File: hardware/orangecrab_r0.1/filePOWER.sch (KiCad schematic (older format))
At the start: 5 parts

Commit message: Initial Routing of Memory Traces. Wired up DCDC converters.
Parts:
- removed U? (x2): FAN53601, symbol gkl_pmic:FAN53601
- added C10: 0.22uF, Capacitor_SMD:C_0201_0603Metric, symbol Device:C
- added C11, C15, C16, C17, C18, C6, C7, C8: 10uF, Capacitor_SMD:C_0402_1005Metric, symbol Device:C
- added C12, C13: 4.7uF, Capacitor_SMD:C_0402_1005Metric, symbol Device:C
- added C14, C2, C5: 10nF, Capacitor_SMD:C_0201_0603Metric, symbol Device:C
- added C3: 10uF, Capacitor_SMD:C_0603_1608Metric, symbol Device:C
- added C9: 0.1uF, Capacitor_SMD:C_0201_0603Metric, symbol Device:C
- added D2: RED, symbol Device:LED_ALT
- added D3: GREEN, symbol Device:LED_ALT
- added L1, L2, L3: 470uH, Inductor_SMD:L_0805_2012Metric, symbol Device:L_Small
- added R1, R13, R14, R17, R18, R5: 100k, Resistor_SMD:R_0201_0603Metric, symbol Device:R
- added R10, R11, R12, R9: 0, symbol Device:R
- added R15, R16, R2: 115k, Resistor_SMD:R_0201_0603Metric, symbol Device:R
- added R6: 0R, symbol Device:R
- added R7, R8: 1k5, symbol Device:R
- added U1, U2, U7: FAN53541, Package_CSP:WLCSP-20_1.934x2.434mm_Layout4x5_P0.4mm, symbol gkl_pmic:FAN53541
- added U8: TPS51206, Package_DFN_QFN:DFN-10-1EP_3x3mm_P0.5mm_EP1.7x2.5mm, symbol gkl_pmic:TPS51206
- U5: renamed from U?; footprint (none) -> Package_DFN_QFN:QFN-16-1EP_3x3mm_P0.5mm_EP1.75x1.75mm
- gave numbers to parts that had none: 2
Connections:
- net labels added: GND, P1.1V, P1.5V, P3.3V, PGOOD_LAST, PGOOD_P1.1V, USB_DN, USB_DP, VSYS, VTT, VTT_REF
- wire segments 0 -> 286
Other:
- note added: "1.5V @ 5A\n- DDR3\n"
- note added: "3.3V @ 5A\n- System IO\n"
- note added: "DDR3 VTT Generator"
- note removed: "1.1V @ 1A"
- note removed: "1.35V @ 1A"
- moved on the sheet: J3, J5, U5

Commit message: Routed more FPGA signals
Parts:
- J3: footprint (none) -> Connector_USB:USB_Micro-B_Molex-105017-0001
- R10, R11, R12, R7, R8, R9: footprint (none) -> Resistor_SMD:R_0201_0603Metric
- R6: footprint (none) -> Resistor_SMD:R_0402_1005Metric
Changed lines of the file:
@@
 F 0 "R6" V 1493 5950 50  0000 C CNN
 F 1 "0R" V 1584 5950 50  0000 C CNN
-F 2 "" V 1630 5950 50  0001 C CNN
+F 2 "Resistor_SMD:R_0402_1005Metric" V 1630 5950 50  0001 C CNN
 F 3 "~" H 1700 5950 50  0001 C CNN
 	1    1700 5950
@@
 F 0 "R8" V 2815 900 50  0000 C CNN
 F 1 "1k5" V 2906 900 50  0000 C CNN
-F 2 "" V 2630 900 50  0001 C CNN
+F 2 "Resistor_SMD:R_0201_0603Metric" V 2630 900 50  0001 C CNN
 F 3 "~" H 2700 900 50  0001 C CNN
 	1    2700 900
@@
 F 0 "R7" V 2493 800 50  0000 C CNN
 F 1 "1k5" V 2584 800 50  0000 C CNN
-F 2 "" V 2630 800 50  0001 C CNN
+F 2 "Resistor_SMD:R_0201_0603Metric" V 2630 800 50  0001 C CNN
 F 3 "~" H 2700 800 50  0001 C CNN
 	1    2700 800
@@
 F 0 "J3" H 1057 2067 50  0000 C CNN
 F 1 "USB_B_Micro" H 1057 1976 50  0000 C CNN
-F 2 "" H 1150 1550 50  0001 C CNN
+F 2 "Connector_USB:USB_Micro-B_Molex-105017-0001" H 1150 1550 50  0001 C CNN
 F 3 "~" H 1150 1550 50  0001 C CNN
 	1    1000 1600
@@
 F 0 "R9" H 3681 2804 50  0000 R CNN
 F 1 "0" H 3681 2895 50  0000 R CNN
-F 2 "" V 3680 2850 50  0001 C CNN
+F 2 "Resistor_SMD:R_0201_0603Metric" V 3680 2850 50  0001 C CNN
 F 3 "~" H 3750 2850 50  0001 C CNN
 	1    3750 2850
@@
 F 0 "R10" H 3881 3054 50  0000 R CNN
 F 1 "0" H 3881 3145 50  0000 R CNN
-F 2 "" V 3880 3100 50  0001 C CNN
+F 2 "Resistor_SMD:R_0201_0603Metric" V 3880 3100 50  0001 C CNN
 F 3 "~" H 3950 3100 50  0001 C CNN
 	1    3950 3100
@@
 F 0 "R11" H 4081 2804 50  0000 R CNN
 F 1 "0" H 4081 2895 50  0000 R CNN
-F 2 "" V 4080 2850 50  0001 C CNN
+F 2 "Resistor_SMD:R_0201_0603Metric" V 4080 2850 50  0001 C CNN
 F 3 "~" H 4150 2850 50  0001 C CNN
 	1    4150 2850
@@
 F 0 "R12" H 4281 3054 50  0000 R CNN
 F 1 "0" H 4281 3145 50  0000 R CNN
-F 2 "" V 4280 3100 50  0001 C CNN
+F 2 "Resistor_SMD:R_0201_0603Metric" V 4280 3100 50  0001 C CNN
 F 3 "~" H 4350 3100 50  0001 C CNN
 	1    4350 3100

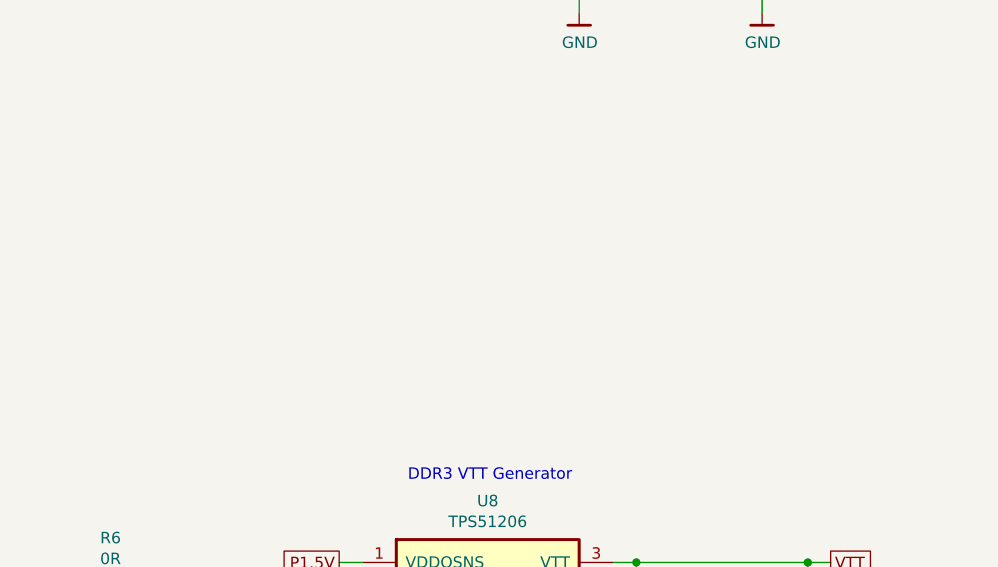
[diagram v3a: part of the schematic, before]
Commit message: Added 2.5V regulator. Completed more routing
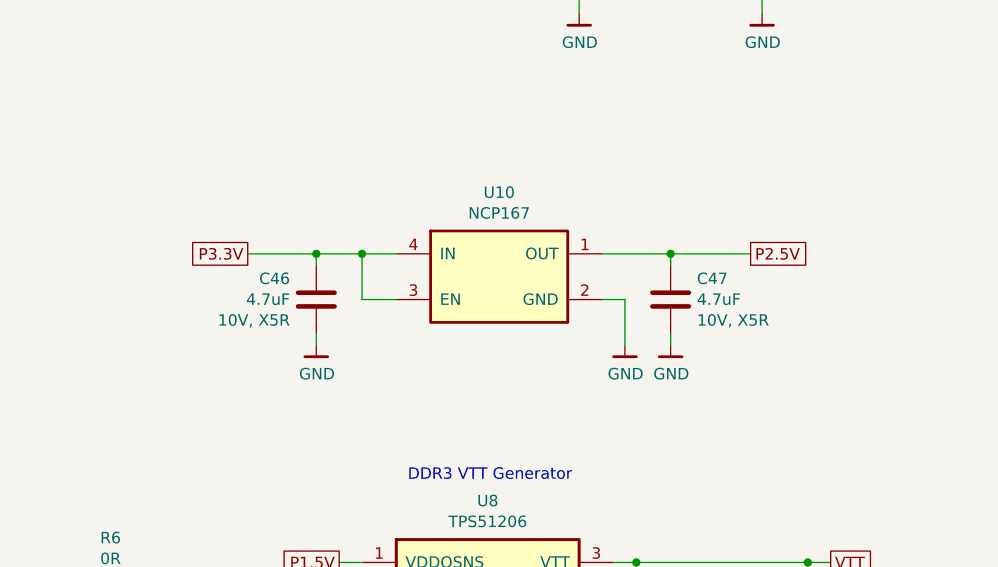
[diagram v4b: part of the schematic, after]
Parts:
- added C46, C47: 4.7uF, Capacitor_SMD:C_0402_1005Metric, symbol Device:C
- added U10: NCP167, gkl_housings_son:X2SON_4_1.0x1.0mm, symbol gkl_pmic:NCP167
- J5: footprint (none) -> gkl_conn:JST_PH_B2B-PH-SM4-TB_1x02-1MP_P2.00mm_Vertical
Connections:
- net GND: now also C46.2, C47.2, U10.2 (GND)
- net P3.3V: now also C46.1, U10.3 (EN), U10.4 (IN)
- new net P2.5V: C47.1, U10.1 (OUT)
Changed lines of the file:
@@
 F 0 "J5" H 5550 2200 50  0000 C CNN
 F 1 "Conn_01x02_Male" H 5300 2100 50  0000 C CNN
-F 2 "" H 5500 1900 50  0001 C CNN
+F 2 "gkl_conn:JST_PH_B2B-PH-SM4-TB_1x02-1MP_P2.00mm_Vertical" H 5500 1900 50  0001 C CNN
 F 3 "~" H 5500 1900 50  0001 C CNN
 	1    5500 1900
@@
 Wire Wire Line
 	7250 5300 7000 5300
+$Comp
+L gkl_pmic:NCP167 U10
+U 1 1 5D75643E
+P 3400 4600
+F 0 "U10" H 3400 4968 50  0000 C CNN
+F 1 "NCP167" H 3400 4877 50  0000 C CNN
+F 2 "gkl_housings_son:X2SON_4_1.0x1.0mm" H 3350 4950 50  0001 C CNN
+F 3 "" H 3400 4850 50  0001 C CNN
+	1    3400 4600
+	1    0    0    -1
+$EndComp
+Text GLabel 2300 4500 0    50   UnSpc ~ 0
+P3.3V
+$Comp
+L Device:C C46
+U 1 1 5D757AA5
+P 2600 4700
+F 0 "C46" H 2715 4791 50  0000 L CNN
+F 1 "4.7uF" H 2715 4700 50  0000 L CNN
+F 2 "Capacitor_SMD:C_0402_1005Metric" H 2638 4550 50  0001 C CNN
+F 3 "~" H 2600 4700 50  0001 C CNN
+F 4 "10V, X5R" H 2715 4609 50  0000 L CNN "Info"
+	1    2600 4700
+	-1   0    0    -1
+$EndComp
+$Comp
+L Device:C C47
+U 1 1 5D7582AA
+P 4150 4700
+F 0 "C47" H 4265 4791 50  0000 L CNN
+F 1 "4.7uF" H 4265 4700 50  0000 L CNN
+F 2 "Capacitor_SMD:C_0402_1005Metric" H 4188 4550 50  0001 C CNN
+F 3 "~" H 4150 4700 50  0001 C CNN
+F 4 "10V, X5R" H 4265 4609 50  0000 L CNN "Info"
+	1    4150 4700
+	1    0    0    -1
+$EndComp
+Text GLabel 4500 4500 2    50   UnSpc ~ 0
+P2.5V
+Wire Wire Line
+	3850 4500 4150 4500
+Wire Wire Line
+	4150 4550 4150 4500
+Connection ~ 4150 4500
+Wire Wire Line
+	4150 4500 4500 4500
+Wire Wire Line
+	2950 4500 2800 4500
+Wire Wire Line
+	2600 4550 2600 4500
+Connection ~ 2600 4500
+Wire Wire Line
+	2600 4500 2300 4500
+Wire Wire Line
+	2600 4850 2600 4900
+Wire Wire Line
+	4150 4850 4150 4900
+Wire Wire Line
+	3850 4700 3950 4700
+Wire Wire Line
+	3950 4700 3950 4900
+Wire Wire Line
+	2950 4700 2800 4700
+Wire Wire Line
+	2800 4700 2800 4500
+Connection ~ 2800 4500
+Wire Wire Line
+	2800 4500 2600 4500
+$Comp
+L gkl_power:GND #PWR0145
+U 1 1 5D85A10F
+P 2600 4900
+F 0 "#PWR0145" H 2600 4650 50  0001 C CNN
+F 1 "GND" H 2603 4774 50  0000 C CNN
+F 2 "" H 2500 4550 50  0001 C CNN
+F 3 "" H 2600 4900 50  0001 C CNN
+	1    2600 4900
+	1    0    0    -1
+$EndComp
+$Comp
+L gkl_power:GND #PWR0146
+U 1 1 5D85A3FC
+P 4150 4900
+F 0 "#PWR0146" H 4150 4650 50  0001 C CNN
+F 1 "GND" H 4153 4774 50  0000 C CNN
+F 2 "" H 4050 4550 50  0001 C CNN
+F 3 "" H 4150 4900 50  0001 C CNN
+	1    4150 4900
+	1    0    0    -1
+$EndComp
+$Comp
+L gkl_power:GND #PWR0147
+U 1 1 5D85A78D
+P 3950 4900
+F 0 "#PWR0147" H 3950 4650 50  0001 C CNN
+F 1 "GND" H 3953 4774 50  0000 C CNN
+F 2 "" H 3850 4550 50  0001 C CNN
+F 3 "" H 3950 4900 50  0001 C CNN
+	1    3950 4900
+	1    0    0    -1
+$EndComp
 $EndSCHEMATC

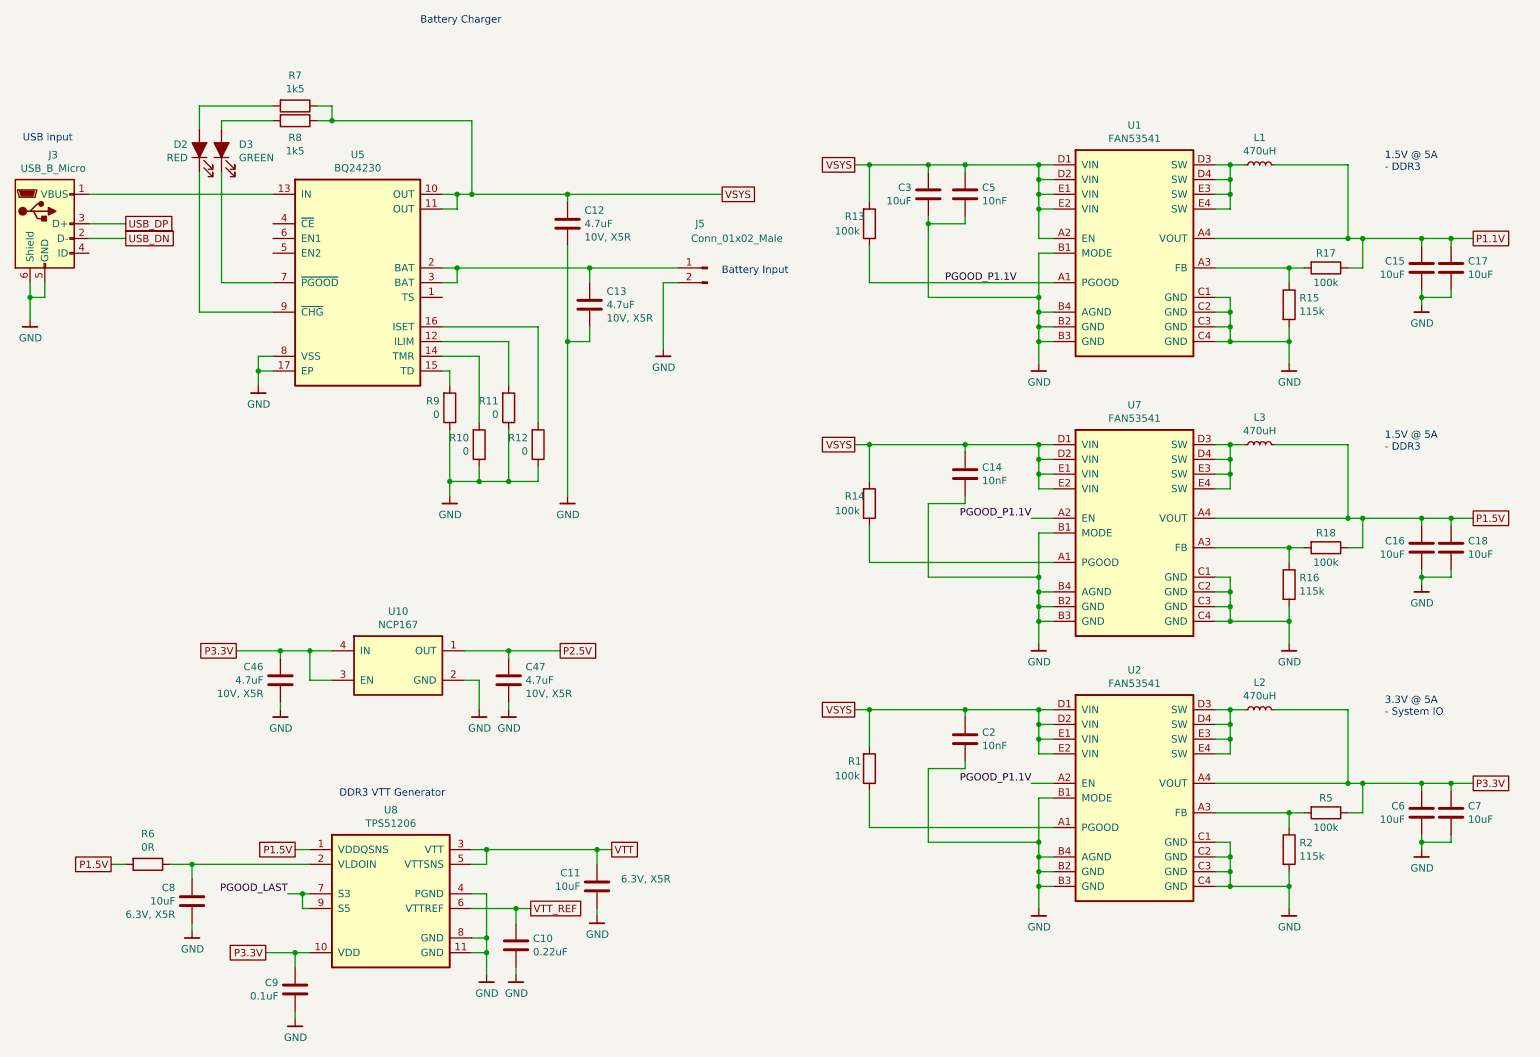
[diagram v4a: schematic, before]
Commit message: Added loads of decoupling capacitors. Added SD card. Started planning out power plane
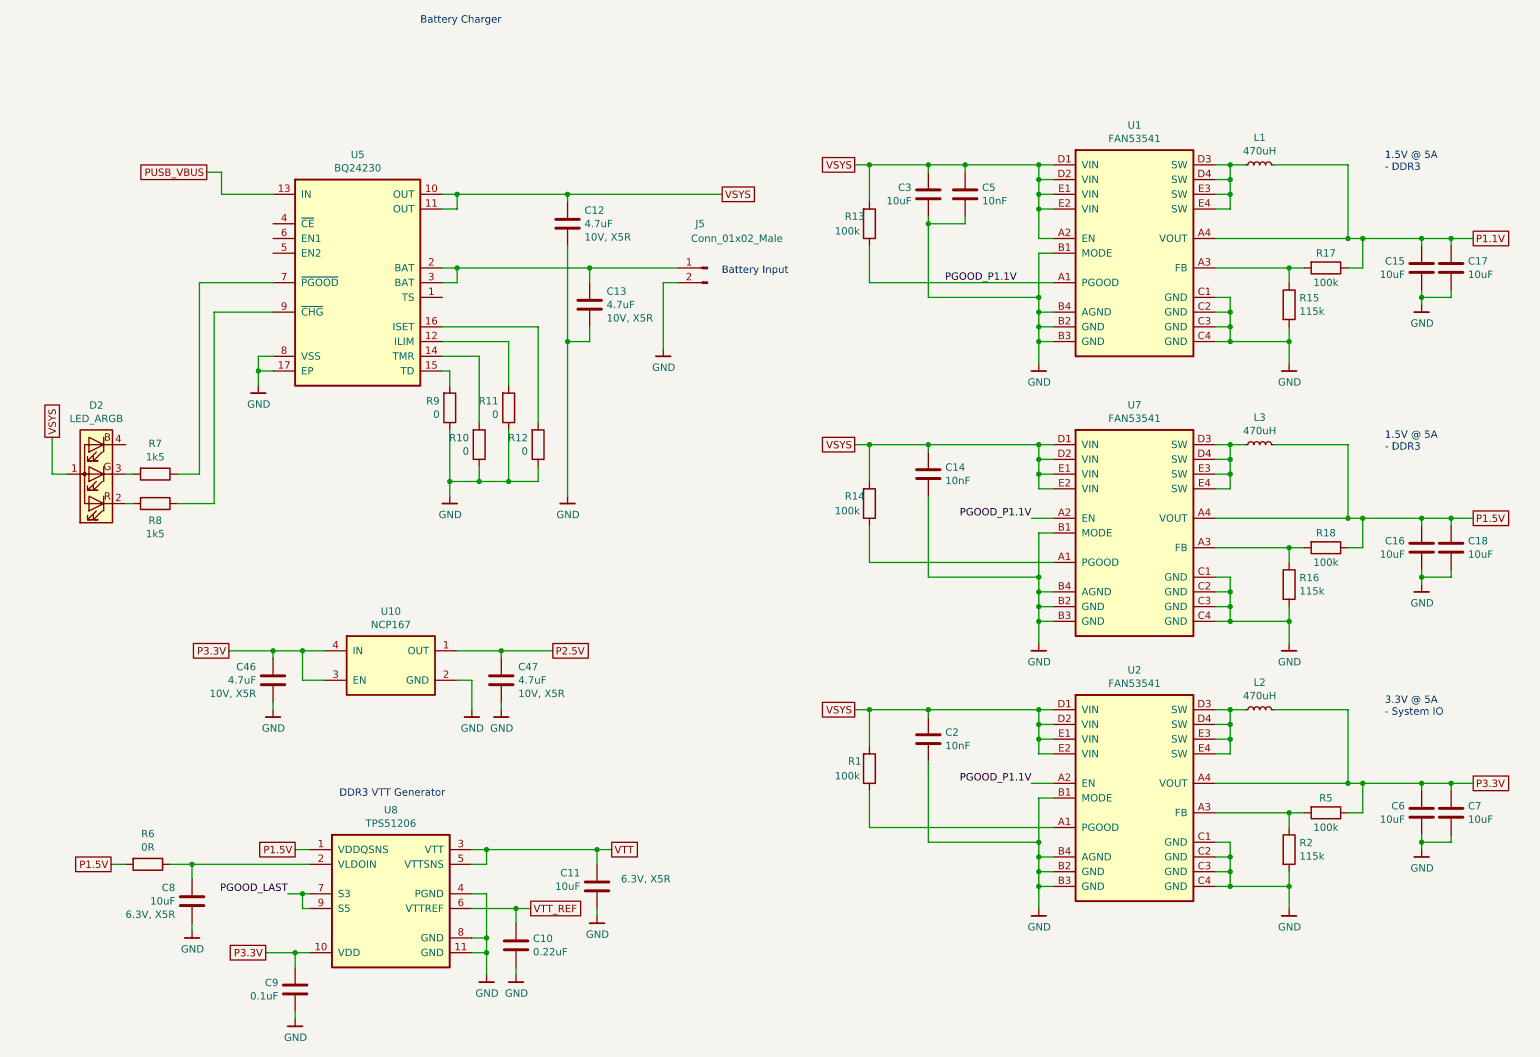
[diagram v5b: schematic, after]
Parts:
- removed D2: RED, symbol Device:LED_ALT
- removed D3: GREEN, symbol Device:LED_ALT
- removed J3: USB_B_Micro, Connector_USB:USB_Micro-B_Molex-105017-0001, symbol Connector:USB_B_Micro
- added D2: LED_ARGB, gkl_led:0404LED_RGB, symbol Device:LED_ARGB
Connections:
- net VSYS: now also D2.1 (A); no longer R7.1, R8.1
- net PUSB_VBUS: now reaches U5.13 (IN)
- net at U5.7 (~PGOOD): now also R7.1
- net at U5.9 (~CHG): now also R8.1
- net at R8.2: now also D2.2 (RK)
- net at R7.2: now also D2.3 (GK)
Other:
- note removed: "USB input"
- moved on the sheet: C14, C2, C46, C47, U10
